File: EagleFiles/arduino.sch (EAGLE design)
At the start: 18 parts, among them IC1 ATMEGA328", IC2 74250N, IC3 74250N, IC4 74250N, IC5 3.3V

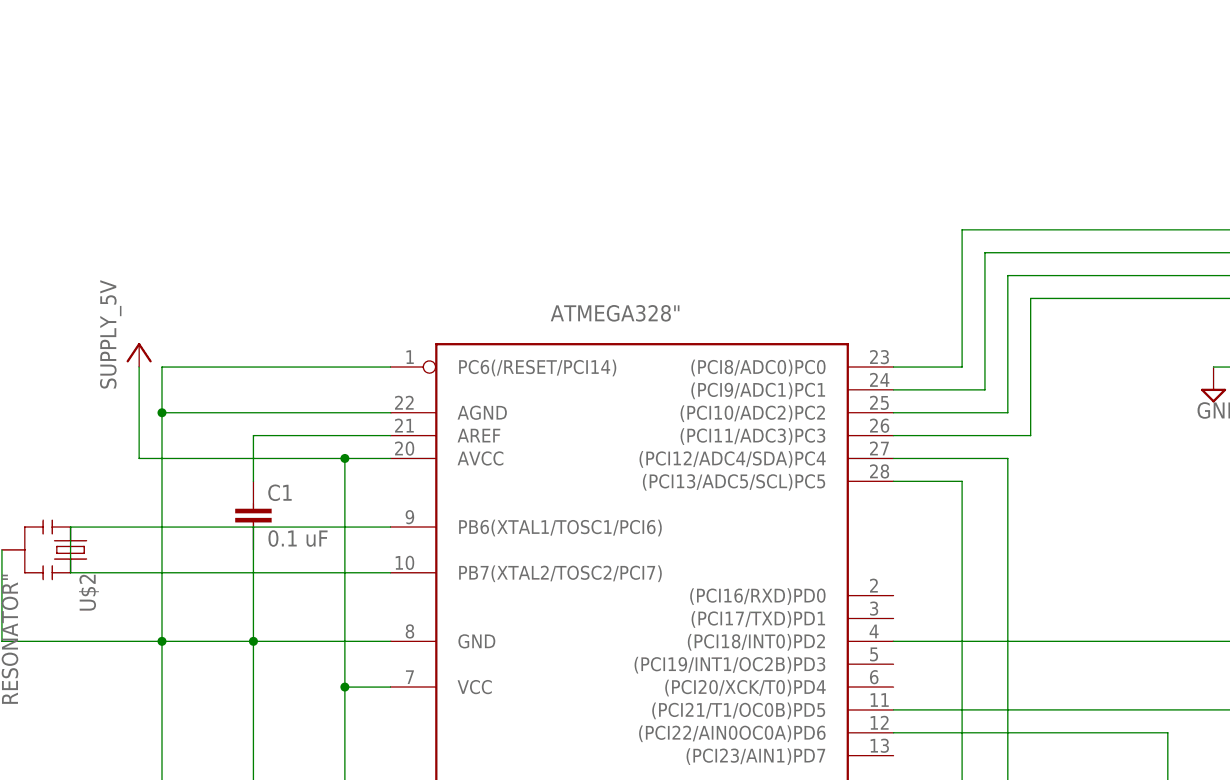
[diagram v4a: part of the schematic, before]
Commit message: added serial interface
- will need use to ftdi cable to use
- do we want to put the ftdi on the
  board so all that is needed is a usb
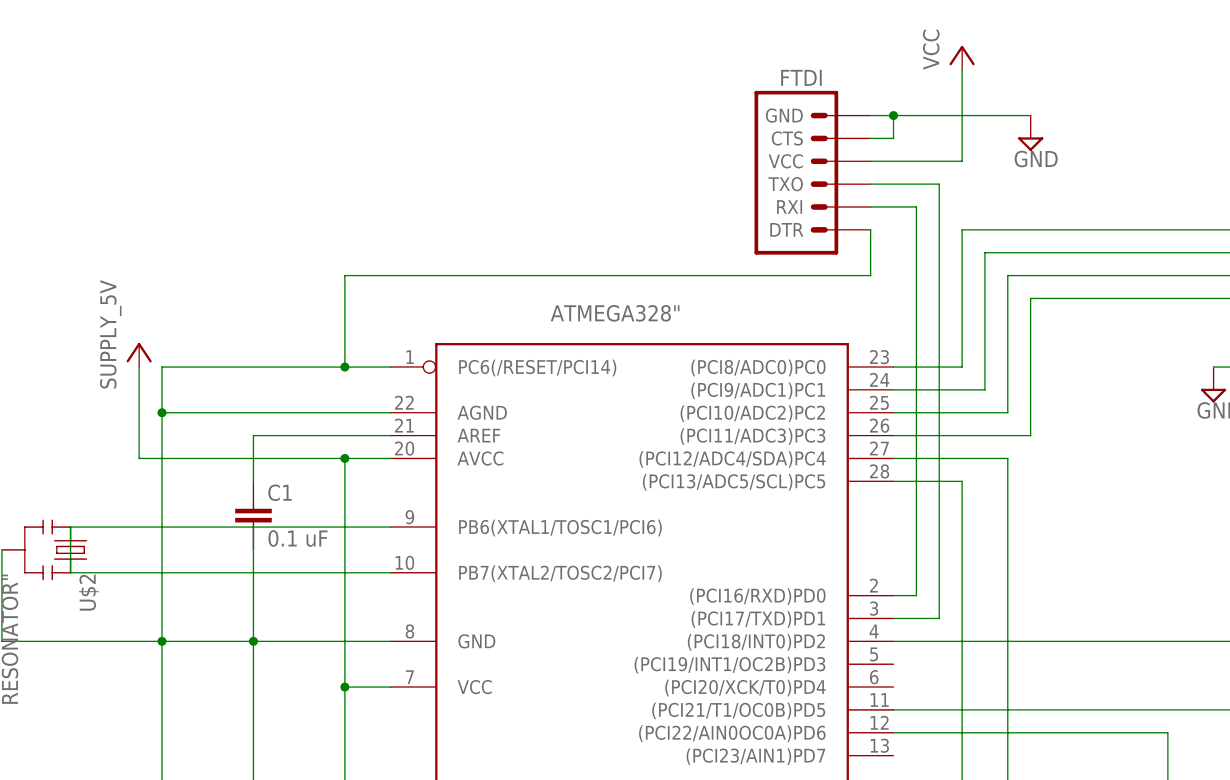
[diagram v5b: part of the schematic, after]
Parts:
- added FTDI: (no value), SparkFun:ARDUINO_SERIAL_PROGRAMPTH
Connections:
- new net N$63: FTDI.RXI, IC1.(PCI16/RXD)PD0
- new net N$66: FTDI.TXO, IC1.(PCI17/TXD)PD1
- new net VCC: FTDI.VCC
- net GND: now also FTDI.CTS, FTDI.DTR, FTDI.GND
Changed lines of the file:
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@@
 <part name="C6" library="SparkFun" deviceset="CAP" device="0402-CAP" value="0.1"/>
 <part name="C7" library="SparkFun" deviceset="CAP" device="0402-CAP"/>
+<part name="FTDI" library="SparkFun" deviceset="ARDUINO_SERIAL_PROGRAM" device="PTH"/>
+<part name="SUPPLY4" library="supply2" deviceset="GND" device=""/>
+<part name="P+1" library="supply1" deviceset="VCC" device=""/>
 </parts>
 <sheets>
@@
 <instance part="C6" gate="G$1" x="71.12" y="12.7" rot="R90"/>
 <instance part="C7" gate="G$1" x="71.12" y="7.62" rot="R90"/>
+<instance part="FTDI" gate="G$1" x="111.76" y="119.38"/>
+<instance part="SUPPLY4" gate="GND" x="134.62" y="124.46"/>
+<instance part="P+1" gate="VCC" x="127" y="134.62"/>
 </instances>
 <busses>
@@
 <wire x1="20.32" y1="68.58" x2="38.1" y2="68.58" width="0.1524" layer="91"/>
 <pinref part="IC1" gate="G$1" pin="PC6(/RESET/PCI14)"/>
-<wire x1="63.5" y1="99.06" x2="38.1" y2="99.06" width="0.1524" layer="91"/>
+<wire x1="63.5" y1="99.06" x2="58.42" y2="99.06" width="0.1524" layer="91"/>
+<wire x1="58.42" y1="99.06" x2="38.1" y2="99.06" width="0.1524" layer="91"/>
 <wire x1="38.1" y1="99.06" x2="38.1" y2="93.98" width="0.1524" layer="91"/>
 <junction x="38.1" y="93.98"/>
@@
 <wire x1="66.04" y1="7.62" x2="66.04" y2="12.7" width="0.1524" layer="91"/>
 <junction x="66.04" y="12.7"/>
+<pinref part="FTDI" gate="G$1" pin="DTR"/>
+<wire x1="116.84" y1="114.3" x2="116.84" y2="109.22" width="0.1524" layer="91"/>
+<wire x1="116.84" y1="109.22" x2="58.42" y2="109.22" width="0.1524" layer="91"/>
+<wire x1="58.42" y1="109.22" x2="58.42" y2="99.06" width="0.1524" layer="91"/>
+<junction x="58.42" y="99.06"/>
 </segment>
 <segment>
@@
 <wire x1="220.98" y1="99.06" x2="154.94" y2="99.06" width="0.1524" layer="91"/>
 <pinref part="SUPPLY3" gate="GND" pin="GND"/>
+</segment>
+<segment>
+<pinref part="FTDI" gate="G$1" pin="GND"/>
+<pinref part="SUPPLY4" gate="GND" pin="GND"/>
+<wire x1="116.84" y1="127" x2="119.38" y2="127" width="0.1524" layer="91"/>
+<wire x1="134.62" y1="127" x2="119.38" y2="127" width="0.1524" layer="91"/>
+<wire x1="119.38" y1="127" x2="119.38" y2="124.46" width="0.1524" layer="91"/>
+<pinref part="FTDI" gate="G$1" pin="CTS"/>
+<wire x1="119.38" y1="124.46" x2="116.84" y2="124.46" width="0.1524" layer="91"/>
+<junction x="119.38" y="127"/>
 </segment>
 </net>
@@
 </segment>
 </net>
+<net name="N$63" class="0">
+<segment>
+<pinref part="IC1" gate="G$1" pin="(PCI16/RXD)PD0"/>
+<wire x1="119.38" y1="73.66" x2="121.92" y2="73.66" width="0.1524" layer="91"/>
+<wire x1="121.92" y1="73.66" x2="121.92" y2="116.84" width="0.1524" layer="91"/>
+<pinref part="FTDI" gate="G$1" pin="RXI"/>
+<wire x1="121.92" y1="116.84" x2="116.84" y2="116.84" width="0.1524" layer="91"/>
+</segment>
+</net>
+<net name="N$66" class="0">
+<segment>
+<pinref part="FTDI" gate="G$1" pin="TXO"/>
+<wire x1="116.84" y1="119.38" x2="124.46" y2="119.38" width="0.1524" layer="91"/>
+<wire x1="124.46" y1="119.38" x2="124.46" y2="71.12" width="0.1524" layer="91"/>
+<pinref part="IC1" gate="G$1" pin="(PCI17/TXD)PD1"/>
+<wire x1="124.46" y1="71.12" x2="119.38" y2="71.12" width="0.1524" layer="91"/>
+</segment>
+</net>
+<net name="VCC" class="0">
+<segment>
+<pinref part="FTDI" gate="G$1" pin="VCC"/>
+<wire x1="116.84" y1="121.92" x2="127" y2="121.92" width="0.1524" layer="91"/>
+<wire x1="127" y1="121.92" x2="127" y2="132.08" width="0.1524" layer="91"/>
+<pinref part="P+1" gate="VCC" pin="VCC"/>
+</segment>
+</net>

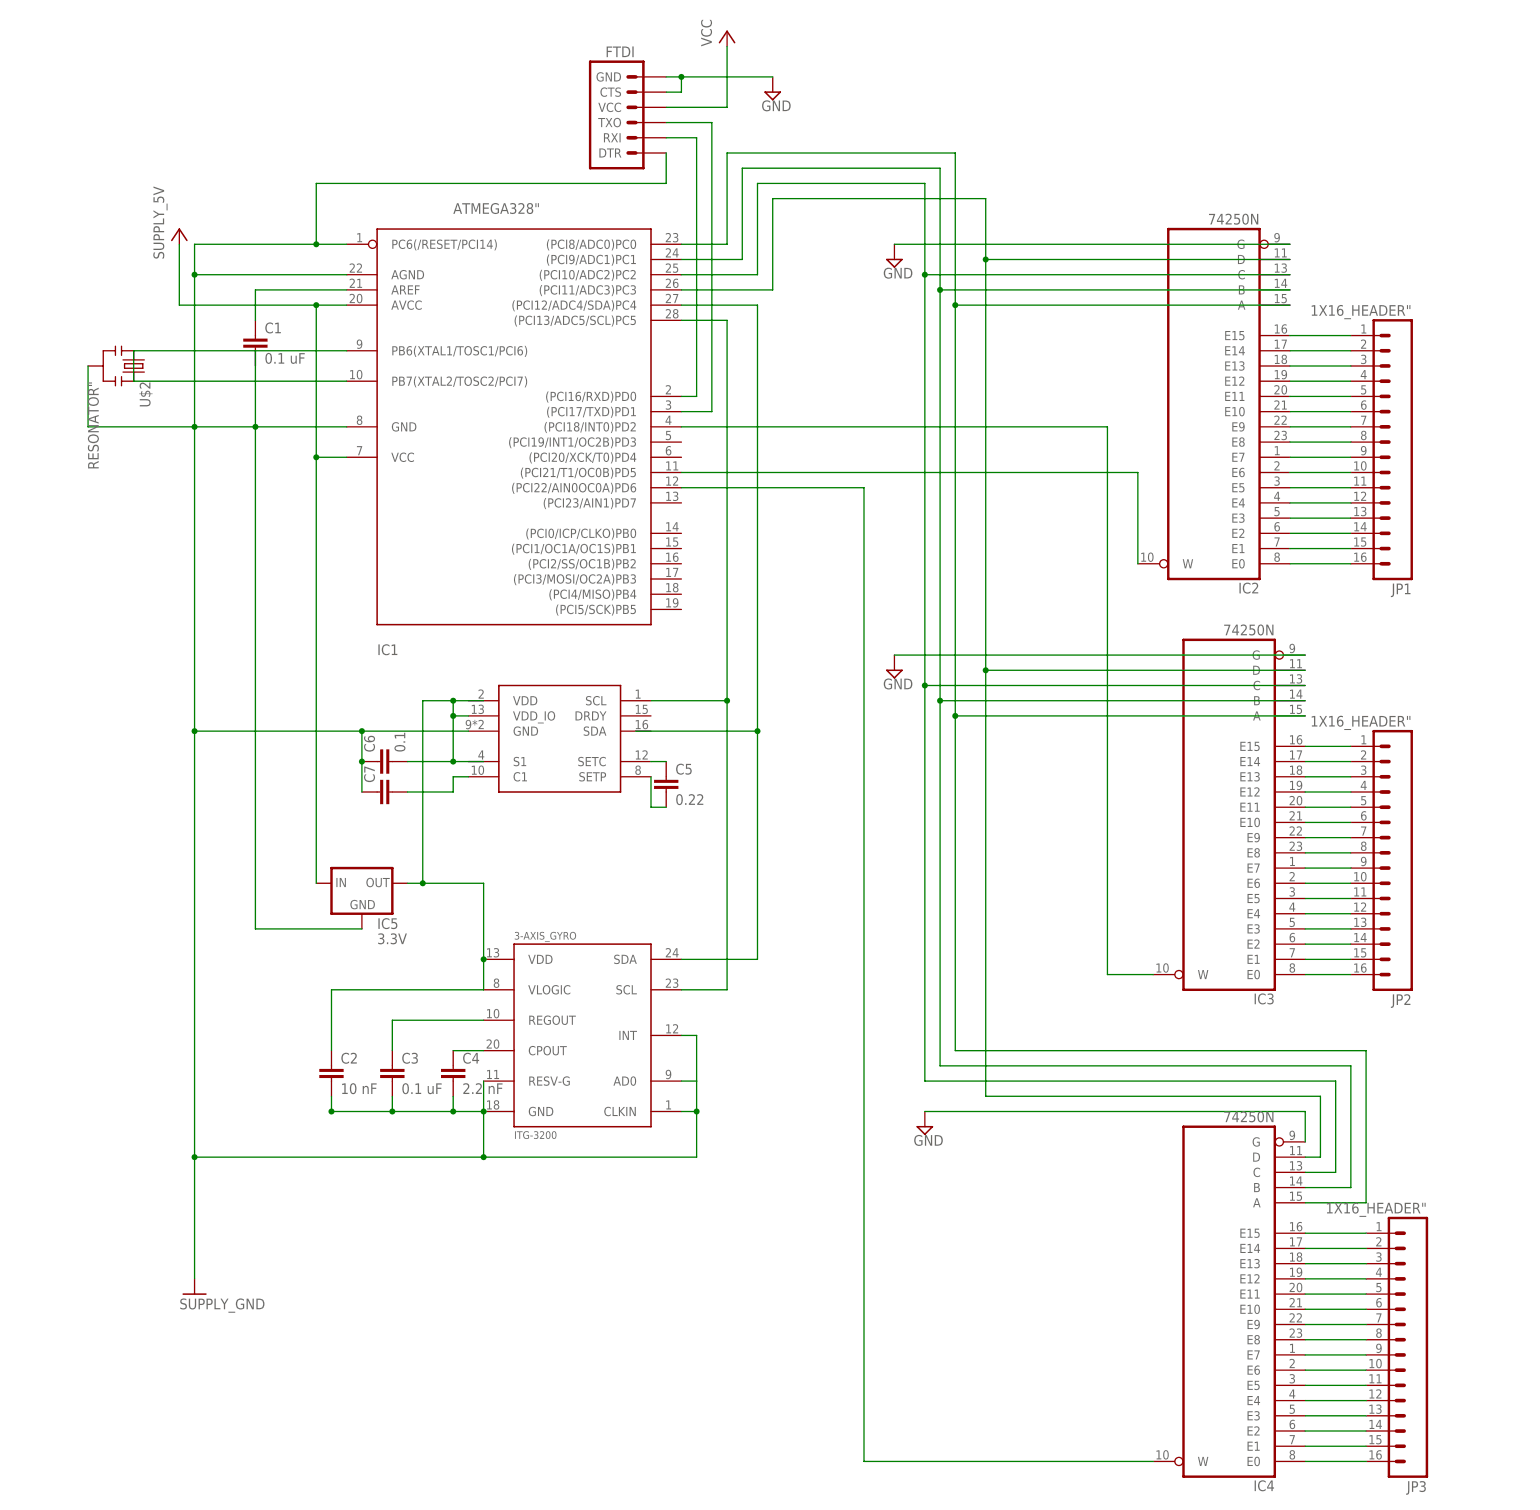
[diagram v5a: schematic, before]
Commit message: changed ATMEG chip +  made the power more right
- the previous atmega used dip (no good)
- new chip us surface mount
- modelled power stuff on the sparkfun razor
  9 degree of freedom imu
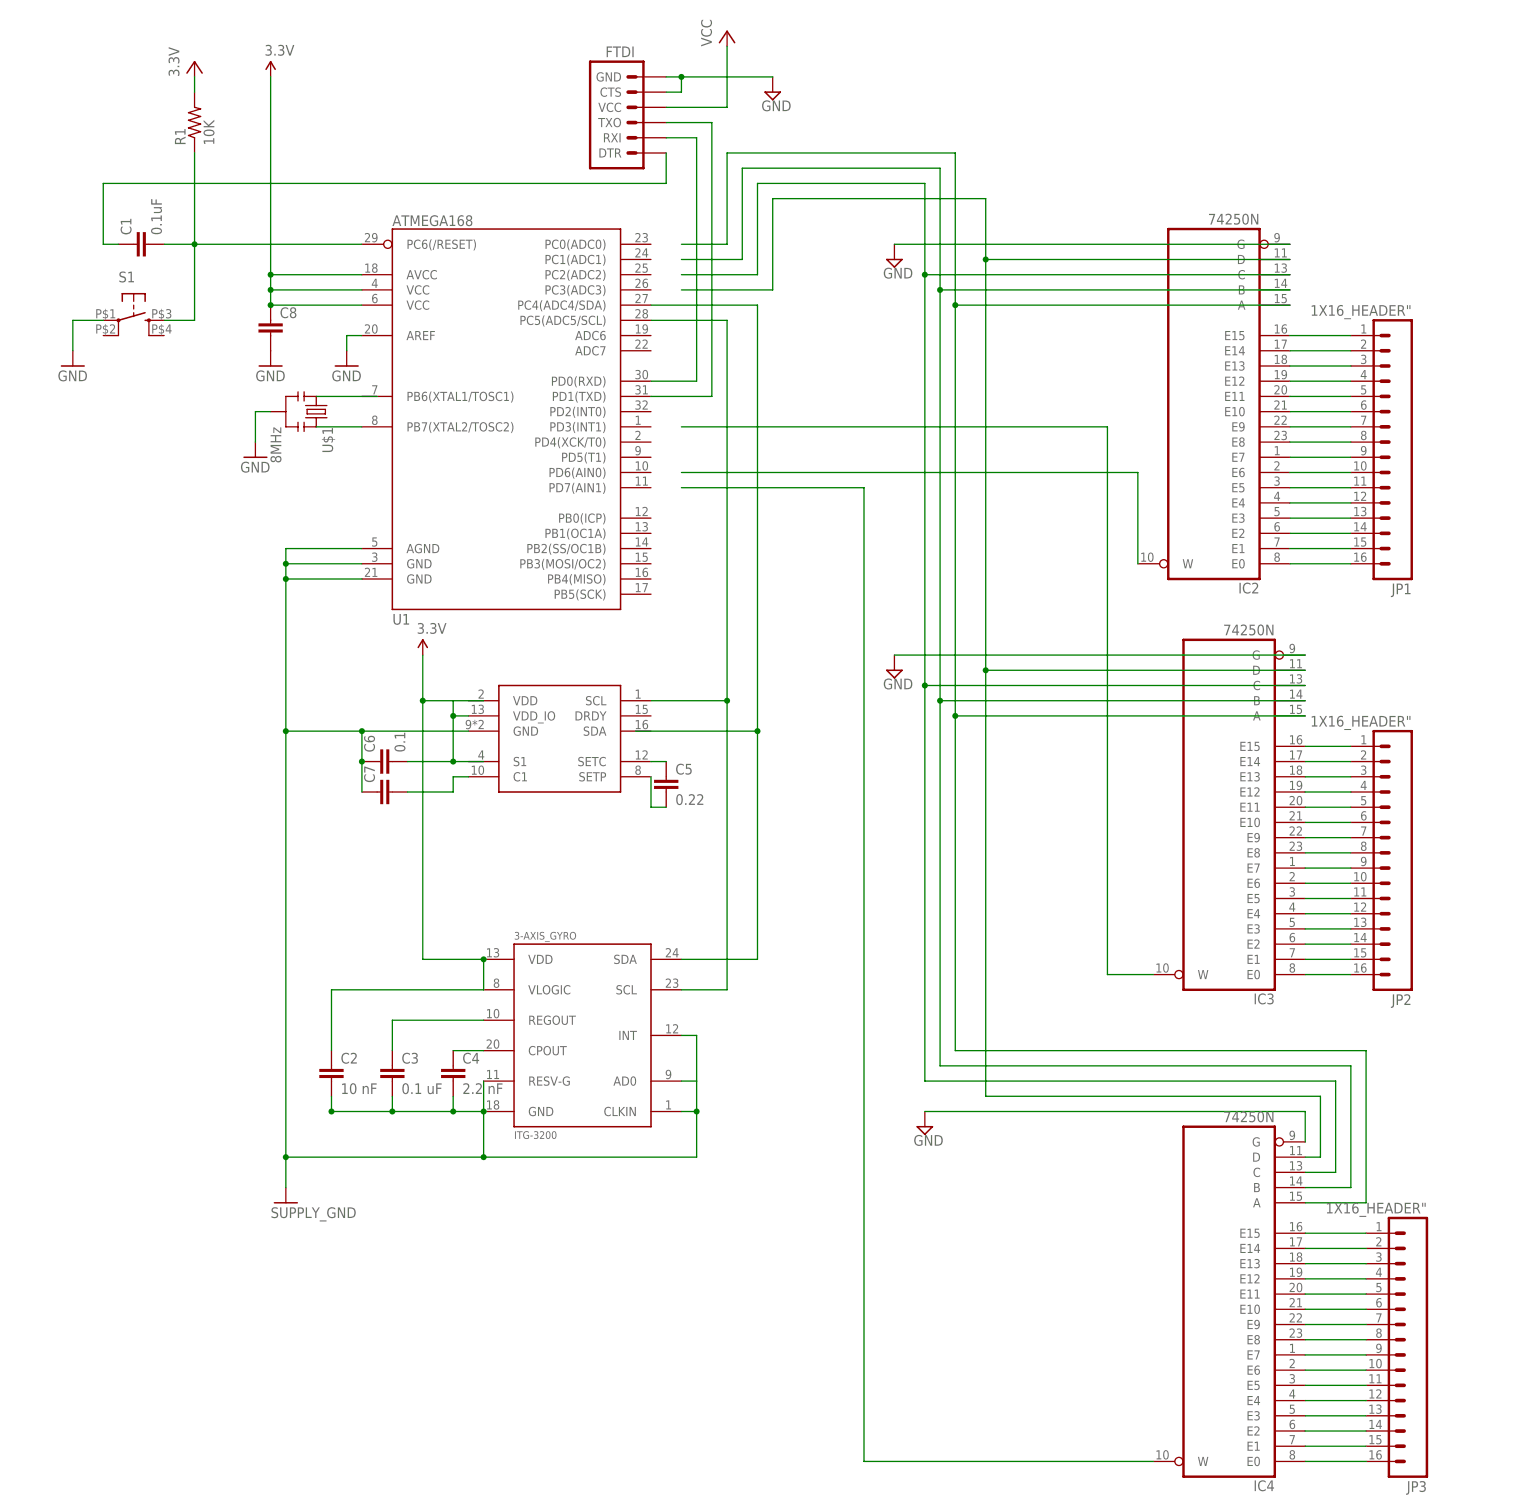
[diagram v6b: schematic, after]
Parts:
- removed IC1: ATMEGA328", RBBB:ATMEGA328"
- removed IC5: 3.3V, RBBB:REGULATOR
- removed U$2: RESONATOR", RBBB:RESONATOR"
- added C8: (no value), SparkFun:CAP0603-CAP
- added R1: 10K, SparkFun:RESISTOR
- added S1: (no value), SparkFun:TAC_SWITCHKSA_SEALED
- added U$1: 8MHz, RBBB:RESONATOR"
- added U1: ATMEGA168, SparkFun:ATMEGA168
- C1: value 0.1 uF -> 0.1uF; device capacitor-wima:C2,5-3 -> SparkFun:CAP0603-CAP
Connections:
- removed net +5V: IC1.AVCC, IC1.VCC, IC5.IN
- removed net N$67: 3-AXIS_GYRO.VDD, 3-AXIS_GYRO.VLOGIC, 3-AXIS_MAG.VDD_IO, C2.1, C6.2, IC5.OUT
- new net N$69: U$1.1
- new net N$70: U$1.3, U1.PB7(XTAL2/TOSC2)
- net GND: now also C8.2, S1.1, U$1.2, U1.AGND, U1.AREF, U1.GND@1, U1.GND@2; no longer FTDI.DTR, IC1.AGND, IC1.GND, IC1.PC6(/RESET/PCI14), IC5.GND, U$2.2
- net N$2: no longer IC1.(PCI10/ADC2)PC2
- net N$3: no longer IC1.(PCI9/ADC1)PC1
- net N$39: now also FTDI.DTR; no longer IC1.AREF
- net N$4: no longer IC1.(PCI8/ADC0)PC0
- net N$40: now also C1.2, R1.1, S1.3, U1.PC6(/RESET); no longer IC1.PB6(XTAL1/TOSC1/PCI6), IC1.PB7(XTAL2/TOSC2/PCI7), U$2.1, U$2.3
- net N$41: now also U1.PC5(ADC5/SCL); no longer IC1.(PCI13/ADC5/SCL)PC5
- net N$42: no longer IC1.(PCI22/AIN0OC0A)PD6
- net N$43: now also U1.PC4(ADC4/SDA); no longer IC1.(PCI12/ADC4/SDA)PC4
- net N$5: no longer IC1.(PCI21/T1/OC0B)PD5
- net N$6: no longer IC1.(PCI18/INT0)PD2
- net N$63: now also U1.PD0(RXD); no longer IC1.(PCI16/RXD)PD0
- net N$66: now also U1.PD1(TXD); no longer IC1.(PCI17/TXD)PD1
- net N$7: no longer IC1.(PCI11/ADC3)PC3
- net VCC: now also 3-AXIS_GYRO.VDD, 3-AXIS_GYRO.VLOGIC, 3-AXIS_MAG.VDD_IO, C2.1, C6.2, C8.1, R1.2, U1.AVCC, U1.VCC@1, U1.VCC@2
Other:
- moved on the sheet: C1
